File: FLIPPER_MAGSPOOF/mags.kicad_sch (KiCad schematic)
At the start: 4 parts, among them J2 Conn_01x10_Socket, J3 Coil, J3 Conn_01x08_Socket, U3 TC4424

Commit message: add BOM and serigraphy
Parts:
- J2: LCSC (none) -> C492418; manf# (none) -> PZ254R-11-10P
- J3: manf# - -> WMRR138F-0
- J3: LCSC (none) -> C2894950; manf# (none) -> PZ254-1-08-W-8.5
- U3: LCSC (none) -> C44150
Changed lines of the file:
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@@
       (effects (font (size 1.27 1.27)) hide)
     )
-    (property "manf#" "-" (at -179.578 157.353 0)
+    (property "manf#" "WMRR138F-0" (at -179.578 157.353 0)
       (effects (font (size 1.27 1.27)) hide)
     )
@@
       (effects (font (size 1.27 1.27)) hide)
     )
+    (property "LCSC" "C2894950" (at 116.713 36.068 0)
+      (effects (font (size 1.27 1.27)) hide)
+    )
+    (property "manf#" "PZ254-1-08-W-8.5" (at 116.713 36.068 0)
+      (effects (font (size 1.27 1.27)) hide)
+    )
+    (pin "1")
+    (pin "2")
+    (pin "3")
+    (pin "4")
+    (pin "5")
+    (pin "6")
+    (pin "7")
     (pin "8")
-    (pin "7")
-    (pin "6")
-    (pin "5")
-    (pin "4")
-    (pin "3")
-    (pin "2")
-    (pin "1")
     (instances
       (project "mags"
@@
       (effects (font (size 1.27 1.27)) hide)
     )
+    (property "manf#" "PZ254R-11-10P" (at 116.459 67.437 0)
+      (effects (font (size 1.27 1.27)) hide)
+    )
+    (property "LCSC" "C492418" (at 116.459 67.437 0)
+      (effects (font (size 1.27 1.27)) hide)
+    )
     (pin "1")
     (pin "10")
@@
       (effects (font (size 1.27 1.27)) hide)
     )
+    (property "LCSC" "C44150" (at 40.513 44.323 0)
+      (effects (font (size 1.27 1.27)) hide)
+    )

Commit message: Change_Coil
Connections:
- net IN_A: now also J3.7 (Pin_2); no longer J3.6 (Pin_3)
- net IN_B: now also J3.6 (Pin_3); no longer J3.5 (Pin_4)
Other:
- note added: "PINOUT DEL FLIPPER ZERO"
- note removed: "PINOUT DEL FLIPPERO ZERO"
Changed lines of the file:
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@@
   (junction (at 107.696 80.137) (diameter 0) (color 0 0 0 0)
   )
+  (no_connect (at 111.633 36.068))
   (no_connect (at 111.379 72.517))
   (no_connect (at 111.379 67.437))
@@
   (no_connect (at 111.633 38.608))
   (no_connect (at 27.813 37.973))
-  (no_connect (at 111.633 30.988))
   (no_connect (at 111.379 64.897))
   (no_connect (at 111.633 43.688))
@@
     (stroke (width 0) (type default))
   )
+  (wire (pts (xy 110.5154 30.988) (xy 111.633 30.988))
+    (stroke (width 0) (type default))
+  )
   (wire (pts (xy 107.696 81.153) (xy 107.696 80.137))
     (stroke (width 0) (type default))
@@
   )
   (wire (pts (xy 54.229 41.783) (xy 53.213 41.783))
-    (stroke (width 0) (type default))
-  )
-  (wire (pts (xy 110.871 36.068) (xy 111.633 36.068))
     (stroke (width 0) (type default))
   )
@@
     (effects (font (size 1 1)) (justify left bottom))
   )
-  (text "PINOUT DEL FLIPPERO ZERO" (at 82.931 19.939 0)
+  (text "PINOUT DEL FLIPPER ZERO" (at 82.931 19.939 0)
     (effects (font (size 3 3)) (justify left bottom))
   )
@@
     (effects (font (size 1.27 1.27)) (justify right bottom))
   )
-  (label "IN_A" (at 110.871 33.528 180) (fields_autoplaced)
+  (label "IN_A" (at 110.5154 30.988 180) (fields_autoplaced)
     (effects (font (size 1.27 1.27)) (justify right bottom))
   )
-  (label "IN_B" (at 110.871 36.068 180) (fields_autoplaced)
+  (label "IN_B" (at 110.871 33.528 180) (fields_autoplaced)
     (effects (font (size 1.27 1.27)) (justify right bottom))
   )

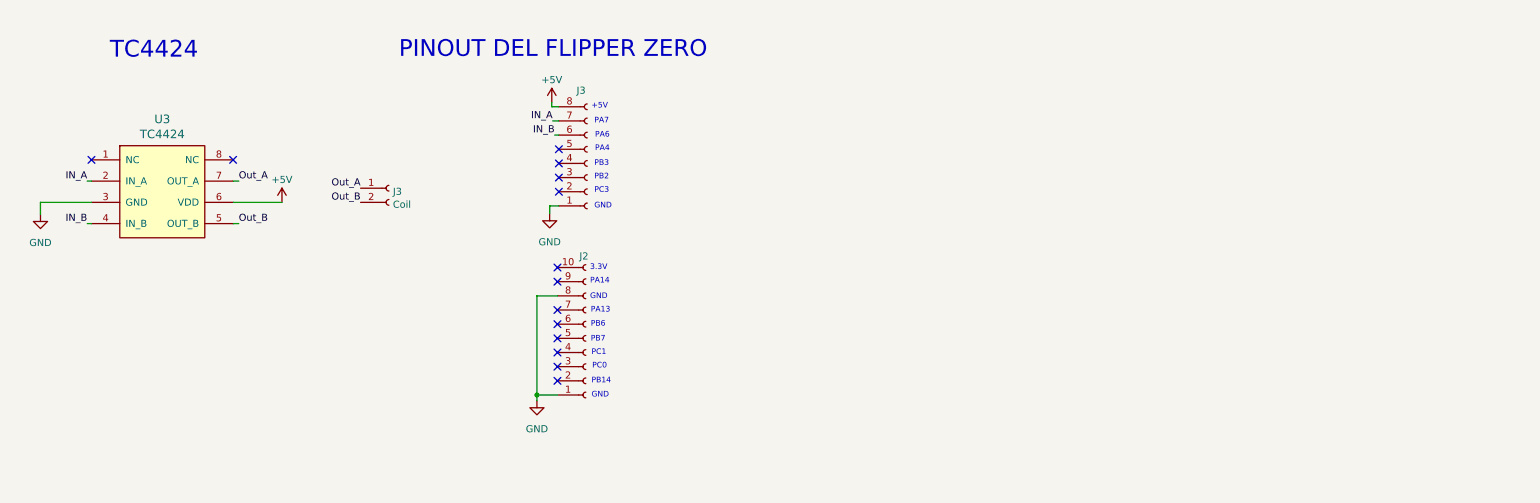
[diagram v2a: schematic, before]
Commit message: Add_Boost
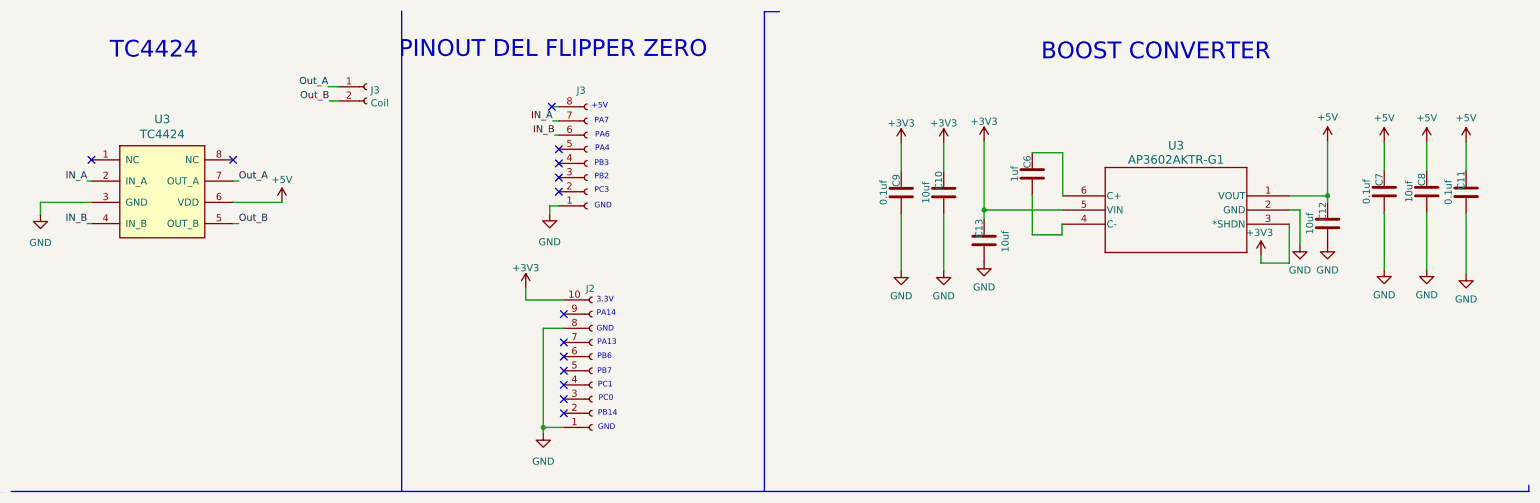
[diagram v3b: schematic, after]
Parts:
- added C10, C12, C13, C8: 10uf, Capacitor_SMD:C_0603_1608Metric_Pad1.08x0.95mm_HandSolder, symbol CanBus-rescue:C-Device
- added C11, C7, C9: 0.1uf, Capacitor_SMD:C_0603_1608Metric_Pad1.08x0.95mm_HandSolder, symbol CanBus-rescue:C-Device
- added C6: 1uf, Capacitor_SMD:C_0603_1608Metric_Pad1.08x0.95mm_HandSolder, symbol CanBus-rescue:C-Device
- added U3: AP3602AKTR-G1, Package_TO_SOT_SMD:TSOT-23-6, symbol 2023-04-21_22-29-41:AP3602AKTR-G1
- J2: LCSC C492418 -> (none); LCSC# (none) -> C492418
- J3: LCSC C2894950 -> (none); LCSC# (none) -> C2894950
- U3: LCSC C44150 -> (none); LCSC# (none) -> C44150
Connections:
- net +5V: now also C11.1, C12.1, C7.1, C8.1, U3.1 (VOUT); no longer J3.8 (Pin_1)
- net GND: now also C10.2, C11.2, C12.2, C13.2, C7.2, C8.2, C9.2, U3.2 (GND)
- net +3V3: now reaches J2.10 (Pin_1)
- net +3V3: now also C10.1, C13.1, C9.1, U3.3 (*SHDN), U3.5 (VIN)
- new net: C6.2, U3.4 (C-)
- new net: C6.1, U3.6 (C+)
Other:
- note added: "BOOST CONVERTER"
- moved on the sheet: J2, J3

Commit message: Add_Pins_Remove_Boost
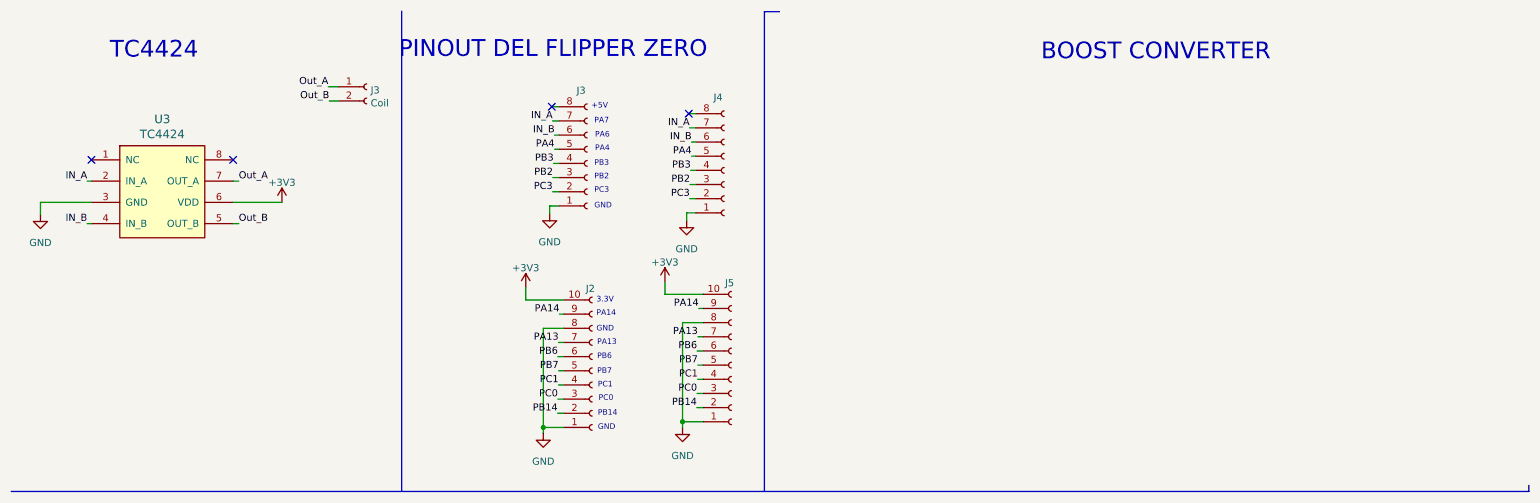
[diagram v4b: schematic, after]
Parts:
- removed C10, C12, C13, C8: 10uf, Capacitor_SMD:C_0603_1608Metric_Pad1.08x0.95mm_HandSolder, symbol CanBus-rescue:C-Device
- removed C11, C7, C9: 0.1uf, Capacitor_SMD:C_0603_1608Metric_Pad1.08x0.95mm_HandSolder, symbol CanBus-rescue:C-Device
- removed C6: 1uf, Capacitor_SMD:C_0603_1608Metric_Pad1.08x0.95mm_HandSolder, symbol CanBus-rescue:C-Device
- removed U3: AP3602AKTR-G1, Package_TO_SOT_SMD:TSOT-23-6, symbol 2023-04-21_22-29-41:AP3602AKTR-G1
- added J4: Conn_01x08_Socket, Connector_PinHeader_2.54mm:PinHeader_1x08_P2.54mm_Vertical, symbol Connector:Conn_01x08_Socket
- added J5: Conn_01x10_Socket, Connector_PinHeader_2.54mm:PinHeader_1x10_P2.54mm_Vertical, symbol Connector:Conn_01x10_Socket
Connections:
- net +5V is gone; now on net +3V3: U3.6 (VDD)
- net +3V3: now also J5.10 (Pin_1)
- net GND: now also J4.1 (Pin_8), J5.1 (Pin_10), J5.8 (Pin_3)
- net IN_A: now also J4.7 (Pin_2)
- net IN_B: now also J4.6 (Pin_3)
- net PC3: now reaches J3.2 (Pin_7)
- net PC3: now also J4.2 (Pin_7)
- net PB2: now reaches J3.3 (Pin_6)
- net PB2: now also J4.3 (Pin_6)
- net PB3: now reaches J3.4 (Pin_5)
- net PB3: now also J4.4 (Pin_5)
- net PA4: now reaches J3.5 (Pin_4)
- net PA4: now also J4.5 (Pin_4)
- net PB14: now reaches J2.2 (Pin_9)
- net PB14: now also J5.2 (Pin_9)
- net PC0: now reaches J2.3 (Pin_8)
- net PC0: now also J5.3 (Pin_8)
- net PC1: now reaches J2.4 (Pin_7)
- net PC1: now also J5.4 (Pin_7)
- net PB7: now reaches J2.5 (Pin_6)
- net PB7: now also J5.5 (Pin_6)
- net PB6: now reaches J2.6 (Pin_5)
- net PB6: now also J5.6 (Pin_5)
- net PA13: now reaches J2.7 (Pin_4)
- net PA13: now also J5.7 (Pin_4)
- net PA14: now reaches J2.9 (Pin_2)
- net PA14: now also J5.9 (Pin_2)
- no-connect marks 14 -> 4

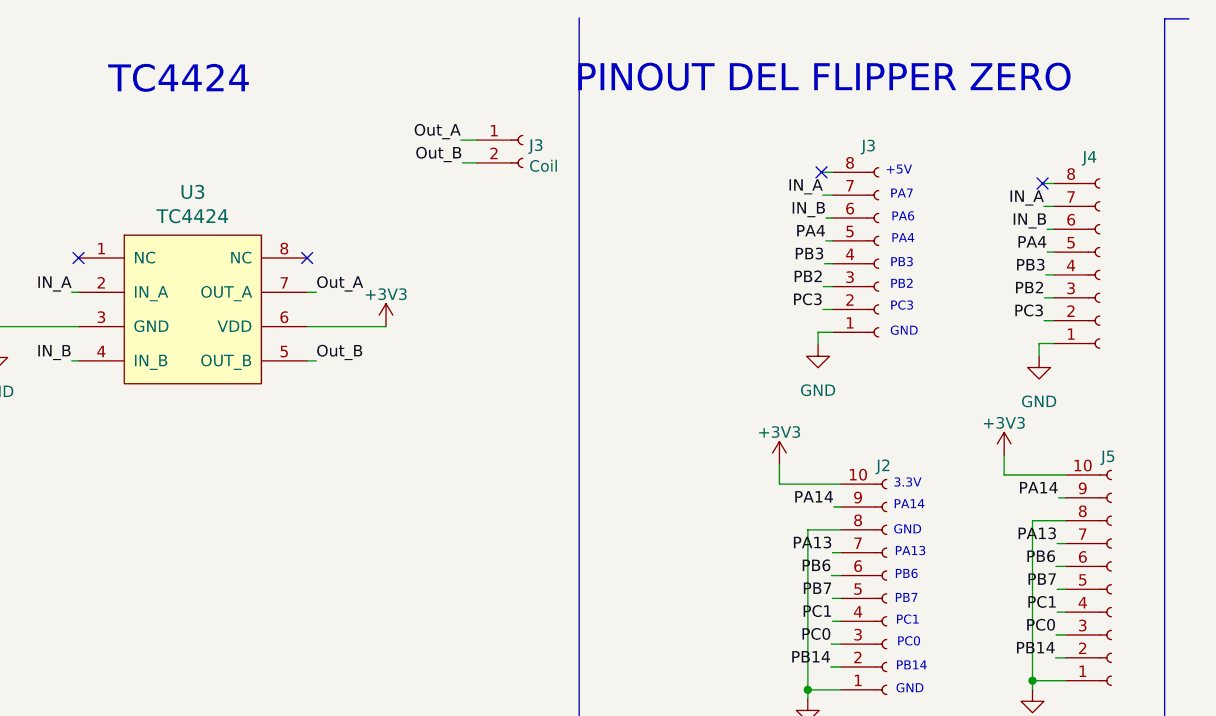
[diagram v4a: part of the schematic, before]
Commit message: Add_SW_3/5v
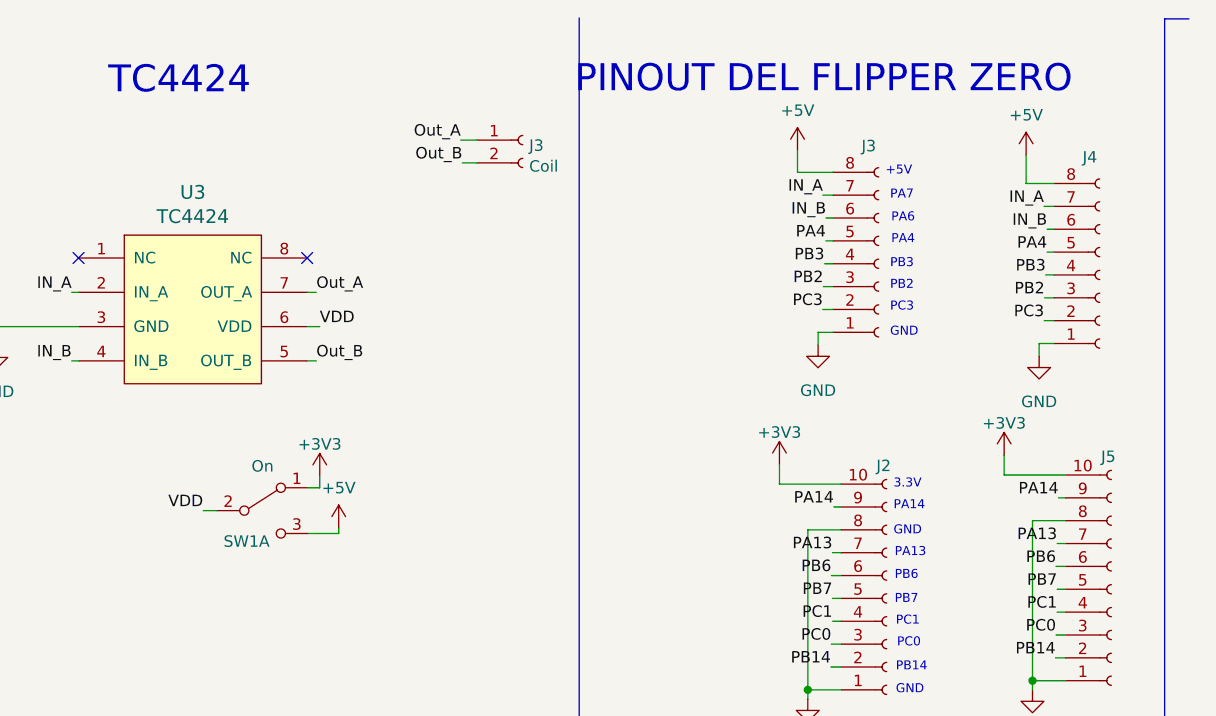
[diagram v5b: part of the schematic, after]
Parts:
- added SW1: On, footprintsg:JS102011SAQN, symbol Switch:SW_DPDT_x2
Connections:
- net +3V3: now also SW1.1 (A); no longer U3.6 (VDD)
- net +5V: now reaches J3.8 (Pin_1)
- net +5V: now also J4.8 (Pin_1), SW1.3 (C)
- new net VDD: SW1.2 (B), U3.6 (VDD)
- no-connect marks 4 -> 2
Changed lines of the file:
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@@
   )
   (no_connect (at 53.213 37.973))
-  (no_connect (at 110.363 28.448))
-  (no_connect (at 134.9248 29.6926))
   (no_connect (at 27.813 37.973))
   (wire (pts (xy 136.5504 74.7776) (xy 137.4902 74.7776))
@@
     (stroke (width 0) (type default))
   )
-  (wire (pts (xy 134.9248 29.6926) (xy 136.1948 29.6926))
+  (wire (pts (xy 133.096 29.6926) (xy 136.1948 29.6926))
     (stroke (width 0) (type default))
   )
@@
     (stroke (width 0) (type default))
   )
+  (wire (pts (xy 56.7182 68.58) (xy 53.34 68.58))
+    (stroke (width 0) (type default))
+  )
   (wire (pts (xy 110.871 33.528) (xy 111.633 33.528))
     (stroke (width 0) (type default))
@@
     (stroke (width 0) (type default))
   )
-  (wire (pts (xy 61.976 45.593) (xy 53.213 45.593))
-    (stroke (width 0) (type default))
-  )
   (polyline (pts (xy 285.5722 96.3422) (xy 285.5722 97.4344))
     (stroke (width 0) (type default))
@@
     (stroke (width 0) (type default))
   )
+  (wire (pts (xy 54.61 62.23) (xy 54.61 63.5))
+    (stroke (width 0) (type default))
+  )
+  (wire (pts (xy 107.696 26.035) (xy 107.696 28.448))
+    (stroke (width 0) (type default))
+  )
+  (wire (pts (xy 53.213 45.593) (xy 54.61 45.593))
+    (stroke (width 0) (type default))
+  )
   (wire (pts (xy 110.5154 43.688) (xy 111.633 43.688))
     (stroke (width 0) (type default))
   )
+  (wire (pts (xy 133.096 26.543) (xy 133.096 29.6926))
+    (stroke (width 0) (type default))
+  )
   (wire (pts (xy 133.8072 85.9536) (xy 133.8072 84.9376))
     (stroke (width 0) (type default))
@@
     (stroke (width 0) (type default))
   )
+  (wire (pts (xy 41.656 66.04) (xy 43.18 66.04))
+    (stroke (width 0) (type default))
+  )
   (wire (pts (xy 135.2804 39.8526) (xy 136.1948 39.8526))
     (stroke (width 0) (type default))
@@
     (stroke (width 0) (type default))
   )
-  (wire (pts (xy 110.363 28.448) (xy 111.633 28.448))
+  (wire (pts (xy 107.696 28.448) (xy 111.633 28.448))
     (stroke (width 0) (type default))
   )
@@
     (stroke (width 0) (type default))
   )
+  (wire (pts (xy 56.7182 67.9704) (xy 56.7182 68.58))
+    (stroke (width 0) (type default))
+  )
   (wire (pts (xy 137.4902 67.1576) (xy 133.8072 67.1576))
     (stroke (width 0) (type default))
@@
   )
   (wire (pts (xy 135.1534 42.3926) (xy 136.1948 42.3926))
+    (stroke (width 0) (type default))
+  )
+  (wire (pts (xy 54.61 63.5) (xy 53.34 63.5))
     (stroke (width 0) (type default))
   )
@@
     (effects (font (size 1.27 1.27)) (justify right bottom))
   )
+  (label "VDD" (at 54.61 45.593 0) (fields_autoplaced)
+    (effects (font (size 1.27 1.27)) (justify left bottom))
+  )
   (label "IN_A" (at 110.5154 30.988 180) (fields_autoplaced)
     (effects (font (size 1.27 1.27)) (justify right bottom))
@@
   )
   (label "IN_B" (at 135.4328 34.7726 180) (fields_autoplaced)
+    (effects (font (size 1.27 1.27)) (justify right bottom))
+  )
+  (label "VDD" (at 41.656 66.04 180) (fields_autoplaced)
     (effects (font (size 1.27 1.27)) (justify right bottom))
   )
@@
         (path "/c000e998-700d-458d-af0b-55d19d346714"
           (reference "#PWR01") (unit 1)
+        )
+      )
+    )
+  )
+  (symbol (lib_id "power:+5V") (at 107.696 26.035 0) (unit 1)
+    (in_bom yes) (on_board yes) (dnp no) (fields_autoplaced)
+    (property "Reference" "#PWR08" (at 107.696 29.845 0)
+      (effects (font (size 1.27 1.27)) hide)
+    )
+    (property "Value" "+5V" (at 107.696 21.59 0)
+      (effects (font (size 1.27 1.27)))
+    )
+    (property "Footprint" "" (at 107.696 26.035 0)
+      (effects (font (size 1.27 1.27)) hide)
+    )
+    (property "Datasheet" "" (at 107.696 26.035 0)
+      (effects (font (size 1.27 1.27)) hide)
+    )
+    (pin "1")
+    (instances
+      (project "mags"
+        (path "/c000e998-700d-458d-af0b-55d19d346714"
+          (reference "#PWR08") (unit 1)
         )
       )
@@
     )
   )
-  (symbol (lib_id "power:+3V3") (at 61.976 45.593 0) (mirror y) (unit 1)
+  (symbol (lib_id "power:+3V3") (at 54.61 62.23 0) (mirror y) (unit 1)
     (in_bom yes) (on_board yes) (dnp no) (fields_autoplaced)
-    (property "Reference" "#PWR021" (at 61.976 49.403 0)
-      (effects (font (size 1.27 1.27)) hide)
-    )
-    (property "Value" "+3V3" (at 61.976 42.037 0)
-      (effects (font (size 1.27 1.27)))
-    )
-    (property "Footprint" "" (at 61.976 45.593 0)
-      (effects (font (size 1.27 1.27)) hide)
-    )
-    (property "Datasheet" "" (at 61.976 45.593 0)
+    (property "Reference" "#PWR021" (at 54.61 66.04 0)
+      (effects (font (size 1.27 1.27)) hide)
+    )
+    (property "Value" "+3V3" (at 54.61 58.674 0)
+      (effects (font (size 1.27 1.27)))
+    )
+    (property "Footprint" "" (at 54.61 62.23 0)
+      (effects (font (size 1.27 1.27)) hide)
+    )
+    (property "Datasheet" "" (at 54.61 62.23 0)
       (effects (font (size 1.27 1.27)) hide)
     )
@@
         (path "/c000e998-700d-458d-af0b-55d19d346714"
           (reference "#PWR02") (unit 1)
+        )
+      )
+    )
+  )
+  (symbol (lib_id "power:+5V") (at 133.096 26.543 0) (unit 1)
+    (in_bom yes) (on_board yes) (dnp no) (fields_autoplaced)
+    (property "Reference" "#PWR09" (at 133.096 30.353 0)
+      (effects (font (size 1.27 1.27)) hide)
+    )
+    (property "Value" "+5V" (at 133.096 22.098 0)
+      (effects (font (size 1.27 1.27)))
+    )
+    (property "Footprint" "" (at 133.096 26.543 0)
+      (effects (font (size 1.27 1.27)) hide)
+    )
+    (property "Datasheet" "" (at 133.096 26.543 0)
+      (effects (font (size 1.27 1.27)) hide)
+    )
+    (pin "1")
+    (instances
+      (project "mags"
+        (path "/c000e998-700d-458d-af0b-55d19d346714"
+          (reference "#PWR09") (unit 1)
         )
       )
@@
         (path "/c000e998-700d-458d-af0b-55d19d346714"
           (reference "J4") (unit 1)
+        )
+      )
+    )
+  )
+  (symbol (lib_id "Switch:SW_DPDT_x2") (at 48.26 66.04 0) (unit 1)
+    (in_bom yes) (on_board yes) (dnp no)
+    (property "Reference" "SW1" (at 46.482 69.469 0)
+      (effects (font (size 1.27 1.27)))
+    )
+    (property "Value" "On" (at 48.26 61.1124 0)
+      (effects (font (size 1.27 1.27)))
+    )
+    (property "Footprint" "footprintsg:JS102011SAQN" (at 48.26 66.04 0)
+      (effects (font (size 1.27 1.27)) hide)
+    )
+    (property "Datasheet" "~" (at 48.26 66.04 0)
+      (effects (font (size 1.27 1.27)) hide)
+    )
+    (property "LCSC#" "" (at 48.26 66.04 0)
+      (effects (font (size 1.27 1.27)) hide)
+    )
+    (property "manf#" "JS102011SAQN" (at 48.26 66.04 0)
+      (effects (font (size 1.27 1.27)) hide)
+    )
+    (pin "1")
+    (pin "2")
+    (pin "3")
+    (pin "4")
+    (pin "5")
+    (pin "6")
+    (instances
+      (project "AjoloteBoard"
+        (path "/7f3eb118-a20c-4239-b800-c9211c66847d"
+          (reference "SW1") (unit 1)
+        )
+      )
+      (project "mags"
+        (path "/c000e998-700d-458d-af0b-55d19d346714"
+          (reference "SW1") (unit 1)
         )
       )
@@
         )
       )
+    )
+  )
+  (symbol (lib_id "power:+5V") (at 56.7182 67.9704 0) (unit 1)
+    (in_bom yes) (on_board yes) (dnp no) (fields_autoplaced)
+    (property "Reference" "#PWR010" (at 56.7182 71.7804 0)
+      (effects (font (size 1.27 1.27)) hide)
+    )
+    (property "Value" "+5V" (at 56.7182 63.5254 0)
+      (effects (font (size 1.27 1.27)))
+    )
+    (property "Footprint" "" (at 56.7182 67.9704 0)
+      (effects (font (size 1.27 1.27)) hide)
+    )
+    (property "Datasheet" "" (at 56.7182 67.9704 0)
+      (effects (font (size 1.27 1.27)) hide)
+    )
+    (pin "1")
+    (instances
+      (project "mags"
+        (path "/c000e998-700d-458d-af0b-55d19d346714"
+          (reference "#PWR010") (unit 1)
+        )
+      )
